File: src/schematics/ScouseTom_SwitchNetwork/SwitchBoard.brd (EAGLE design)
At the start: 169.5 x 97.5 mm, 87 parts, among them T1 PNP, U1 MCP73831, U10 ADG714BRUZ, U11 ADG714BRUZ, U12 ADUM1410ARWZ, U13 ADG714BRUZ, U14 ADG714BRUZ, U15 ADUM1412ARWZ, U2 ADG714BRUZ, U3 ADG714BRUZ, U4 TPS61090RSAR, U5 ADG714BRUZ, U6 ADG714BRUZ, U7 ADG714BRUZ, U8 LT1763CDE-5, U9 ADG714BRUZ, X2 CTR_ARD, X3 CTR_OUT, X4 DSUB _T, X5 DSUB_B, X6 CTR_IN

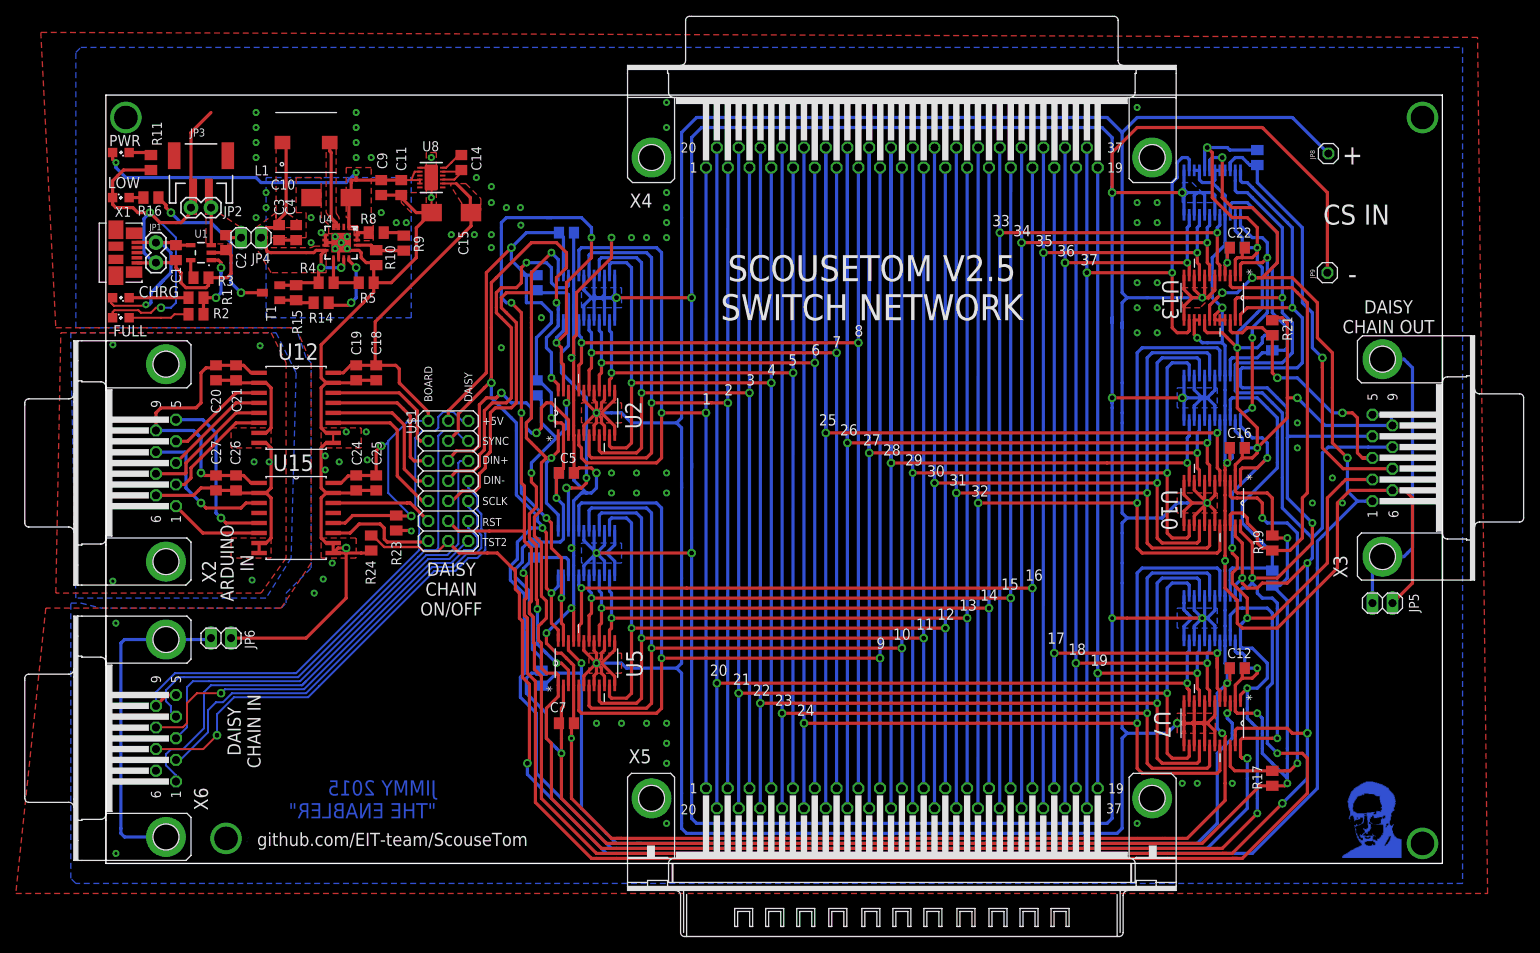
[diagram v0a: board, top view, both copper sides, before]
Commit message: Updated Switchboard - pull down resistors, fixed routing, protection diodes and different battery connector
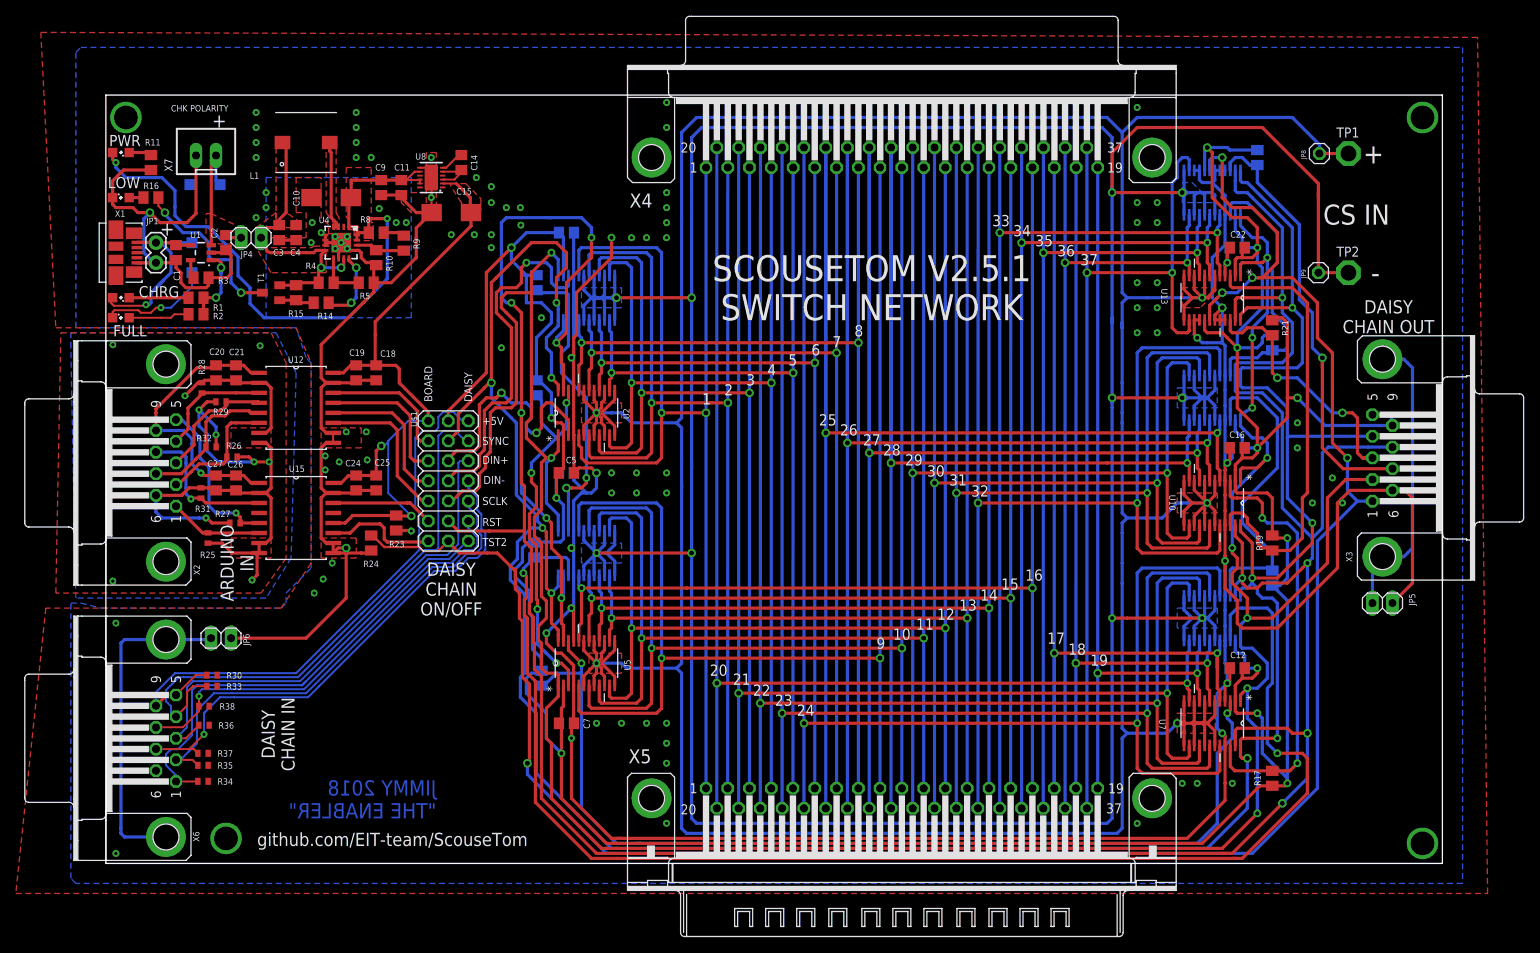
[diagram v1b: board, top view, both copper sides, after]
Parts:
- removed JP2: LiPoIN, SparkFun:1X02
- removed JP3: LiPo, SparkFun:JST-2-SMD
- added D1, D2: 1N4148W-7-F, diode:SOD123
- added R25, R26, R27, R28, R29, R30, R31, R32, R33, R34, R35, R36, R37, R38: 10k, rcl:R0402
- added TP1, TP2: TPPAD1-20, testpad:P1-20
- added X7: JST-XH-02-PIN-LONG-PAD, Rembrandt Electronics - JST XH Connectors v1-0:JST-XH-02-PACKAGE-LONG-PAD
- moved JP8 1.14 mm to (136.8, 94.5)
- moved JP9 1.14 mm to (136.7, 79.4)
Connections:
- net N$12 renamed CTR_IN_SHLD
- net 5VIN: now also D1.C
- net AGND: now also D1.A, D2.A, R30.1, R33.1, R34.1, R35.1, R36.1, R37.1, R38.1, X7.1; no longer JP2.2, JP3.1
- net DIN+_DCHN: now also R36.2
- net DIN+_IN: now also R29.2
- net DIN-_DCHN: now also R37.2
- net DIN-_IN: now also R32.2
- net GND: now also R25.2, R26.2, R27.1, R28.1, R29.1, R31.1, R32.1
- net IN+: now also TP1.TP
- net IN-: now also TP2.TP
- net RESET_IN: now also R31.2
- net SCLK_DCHN: now also R35.2
- net SCLK_IN: now also R26.1
- net SYNC_IN: now also R28.2
- net TEST_1_IN: now also R27.2
- net TEST_2_DCHN: now also R34.2
- net TEST_2_IN: now also R25.1
- net VBATT_A: now also D2.C, X7.2; no longer JP2.1, JP3.2
- net VDD_DCHN: now also R30.2
- net ~RESET_DCHN: now also R38.2
- net ~SYNC_DCHN: now also R33.2
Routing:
- net GND: track 45.9 -> 98.1 mm, vias 6 -> 10
- net VREG: track 56.3 -> 85.1 mm
- net AGND: track 585.6 -> 570.2 mm
- net VBATT_A: track 8.62 -> 17.9 mm
- net ~SYNC_DCHN: track 64.8 -> 71.3 mm
- net SCLK_DCHN: track 58.2 -> 63.5 mm
- net VDD_DCHN: track 69.5 -> 74.5 mm
- net 5VIN: track 24.6 -> 28.7 mm
- net IN-: track 513.8 -> 517.6 mm
- net TEST_2_DCHN: track 57.1 -> 60.9 mm
- net DIN+_DCHN: track 60.7 -> 64.2 mm
- net +5V: track 39.8 -> 36.2 mm
- net IN+: track 502.1 -> 505.3 mm
- net DIN+_IN: track 13.7 -> 15.5 mm
- net SCLK_IN: track 14.5 -> 16.2 mm
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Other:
- board text added: "CHK POLARITY"
- board text added: "JIMMY 2018 "THE ENABLER""
- board text added: "SCOUSETOM V2.5.1 SWITCH NETWORK"
- board text removed: "JIMMY 2015 "THE ENABLER""
- board text removed: "SCOUSETOM V2.5 SWITCH NETWORK"

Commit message: Gerbers for updated shield, sent to PCBtrain. Minor edits to routing
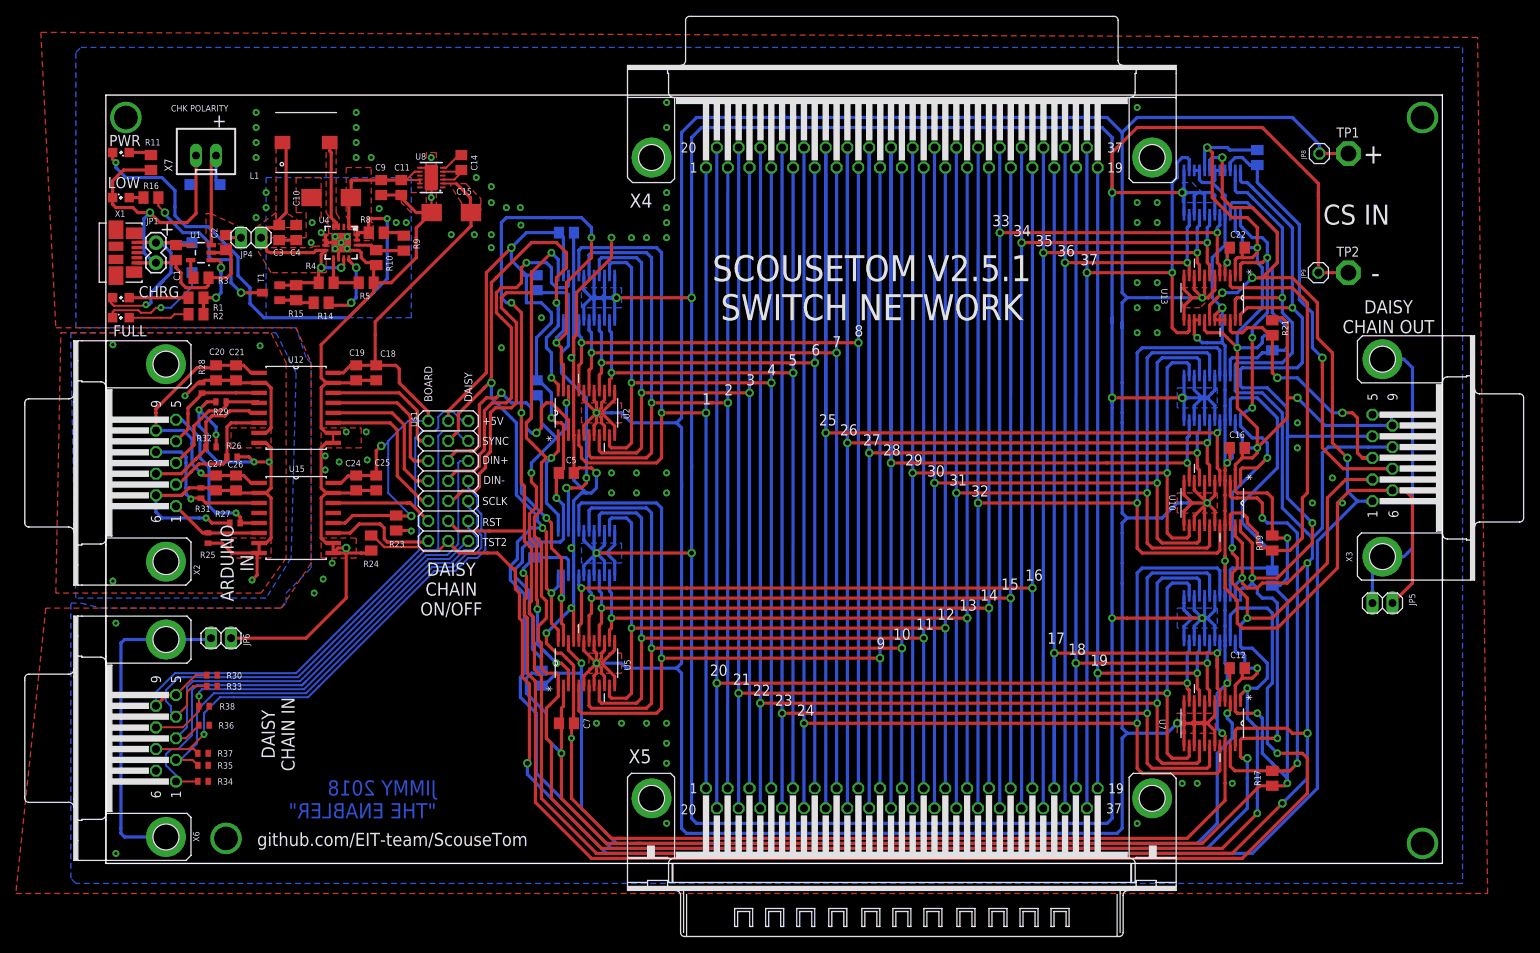
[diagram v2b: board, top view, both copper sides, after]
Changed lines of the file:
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@@
 </class>
 </classes>
-<designrules name="SparkFun-2-layer">
-<description language="en">&lt;b&gt;EAGLE Design Rules&lt;/b&gt;
+<designrules name="pcbtrain">
+<description language="en">&lt;b&gt;PCB TRAIN &lt;i&gt;metric&lt;/i&gt; Design Rules&lt;/b&gt;
 &lt;p&gt;
-The default Design Rules have been set to cover
-a wide range of applications. Your particular design
-may have different requirements, so please make the
-necessary adjustments and save your customized
-design rules under a new name.</description>
+These strictly adhere to the PCB Train board house specs. The rules are &lt;i&gt;metric&lt;/i&gt; so there might be problems with high density chips etc.&lt;p&gt;</description>
 <param name="layerSetup" value="(1*16)"/>
 <param name="mtCopper" value="0.035mm 0.035mm 0.035mm 0.035mm 0.035mm 0.035mm 0.035mm 0.035mm 0.035mm 0.035mm 0.035mm 0.035mm 0.035mm 0.035mm 0.035mm 0.035mm"/>
 <param name="mtIsolate" value="1.5mm 0.15mm 0.2mm 0.15mm 0.2mm 0.15mm 0.2mm 0.15mm 0.2mm 0.15mm 0.2mm 0.15mm 0.2mm 0.15mm 0.2mm"/>
-<param name="mdWireWire" value="8mil"/>
-<param name="mdWirePad" value="8mil"/>
-<param name="mdWireVia" value="8mil"/>
-<param name="mdPadPad" value="8mil"/>
-<param name="mdPadVia" value="8mil"/>
-<param name="mdViaVia" value="8mil"/>
-<param name="mdSmdPad" value="8mil"/>
-<param name="mdSmdVia" value="8mil"/>
-<param name="mdSmdSmd" value="8mil"/>
+<param name="mdWireWire" value="0.2mm"/>
+<param name="mdWirePad" value="0.2mm"/>
+<param name="mdWireVia" value="0.2mm"/>
+<param name="mdPadPad" value="0.2mm"/>
+<param name="mdPadVia" value="0.2mm"/>
+<param name="mdViaVia" value="0.2mm"/>
+<param name="mdSmdPad" value="0mil"/>
+<param name="mdSmdVia" value="0mil"/>
+<param name="mdSmdSmd" value="0mil"/>
 <param name="mdViaViaSameLayer" value="8mil"/>
 <param name="mnLayersViaInSmd" value="2"/>
-<param name="mdCopperDimension" value="8mil"/>
-<param name="mdDrill" value="8mil"/>
+<param name="mdCopperDimension" value="10mil"/>
+<param name="mdDrill" value="0.2mm"/>
 <param name="mdSmdStop" value="0mil"/>
-<param name="msWidth" value="7mil"/>
-<param name="msDrill" value="15mil"/>
+<param name="msWidth" value="0.2mm"/>
+<param name="msDrill" value="0.4mm"/>
 <param name="msMicroVia" value="9.99mm"/>
 <param name="msBlindViaRatio" value="0.5"/>
@@
 <param name="rvMicroViaOuter" value="0.25"/>
 <param name="rvMicroViaInner" value="0.25"/>
-<param name="rlMinPadTop" value="12mil"/>
+<param name="rlMinPadTop" value="10mil"/>
 <param name="rlMaxPadTop" value="20mil"/>
 <param name="rlMinPadInner" value="10mil"/>
 <param name="rlMaxPadInner" value="20mil"/>
-<param name="rlMinPadBottom" value="12mil"/>
+<param name="rlMinPadBottom" value="10mil"/>
 <param name="rlMaxPadBottom" value="20mil"/>
 <param name="rlMinViaOuter" value="10mil"/>
@@
 <param name="mvStopFrame" value="1"/>
 <param name="mvCreamFrame" value="0"/>
-<param name="mlMinStopFrame" value="4mil"/>
-<param name="mlMaxStopFrame" value="4mil"/>
+<param name="mlMinStopFrame" value="0.125mm"/>
+<param name="mlMaxStopFrame" value="0.125mm"/>
 <param name="mlMinCreamFrame" value="0mil"/>
 <param name="mlMaxCreamFrame" value="0mil"/>
-<param name="mlViaStopLimit" value="20mil"/>
+<param name="mlViaStopLimit" value="0mil"/>
 <param name="srRoundness" value="0"/>
 <param name="srMinRoundness" value="0mil"/>
@@
 <param name="dpGapFactor" value="2.5"/>
 <param name="checkGrid" value="0"/>
-<param name="checkAngle" value="1"/>
+<param name="checkAngle" value="0"/>
 <param name="checkFont" value="1"/>
 <param name="checkRestrict" value="1"/>
